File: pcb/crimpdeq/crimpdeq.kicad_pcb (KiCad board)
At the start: 2 copper layers, 23 x 63.8 mm, 49 parts, among them J2 USB4105-GF-A, Q1 SS8550, Q2 DMG3415U, SW1 SW_Push, SW2 SW_Push, U1 ESP32-C3-MINI-1, U2 MCP73831T-2ACI/OT, U3 HX711, U4 Rust_Board, U6 SY8088

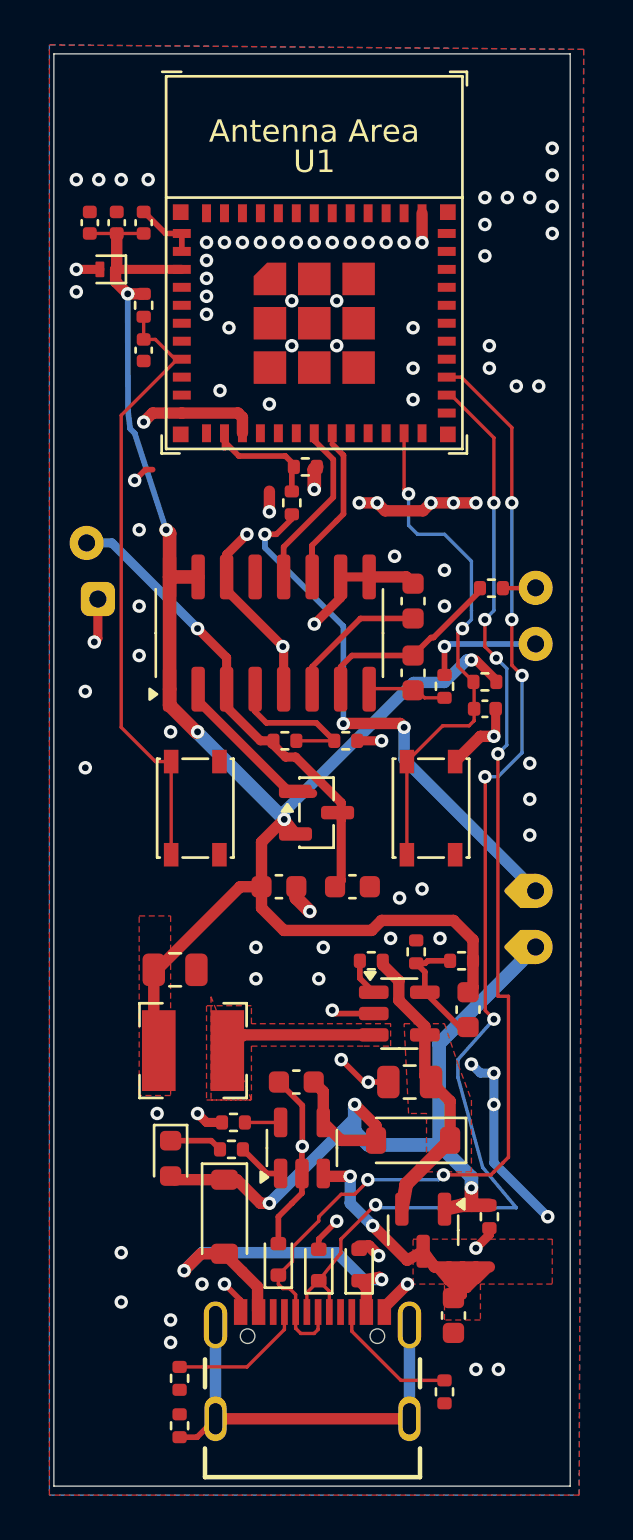
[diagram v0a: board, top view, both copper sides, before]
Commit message: feat: Add rbg led and route it
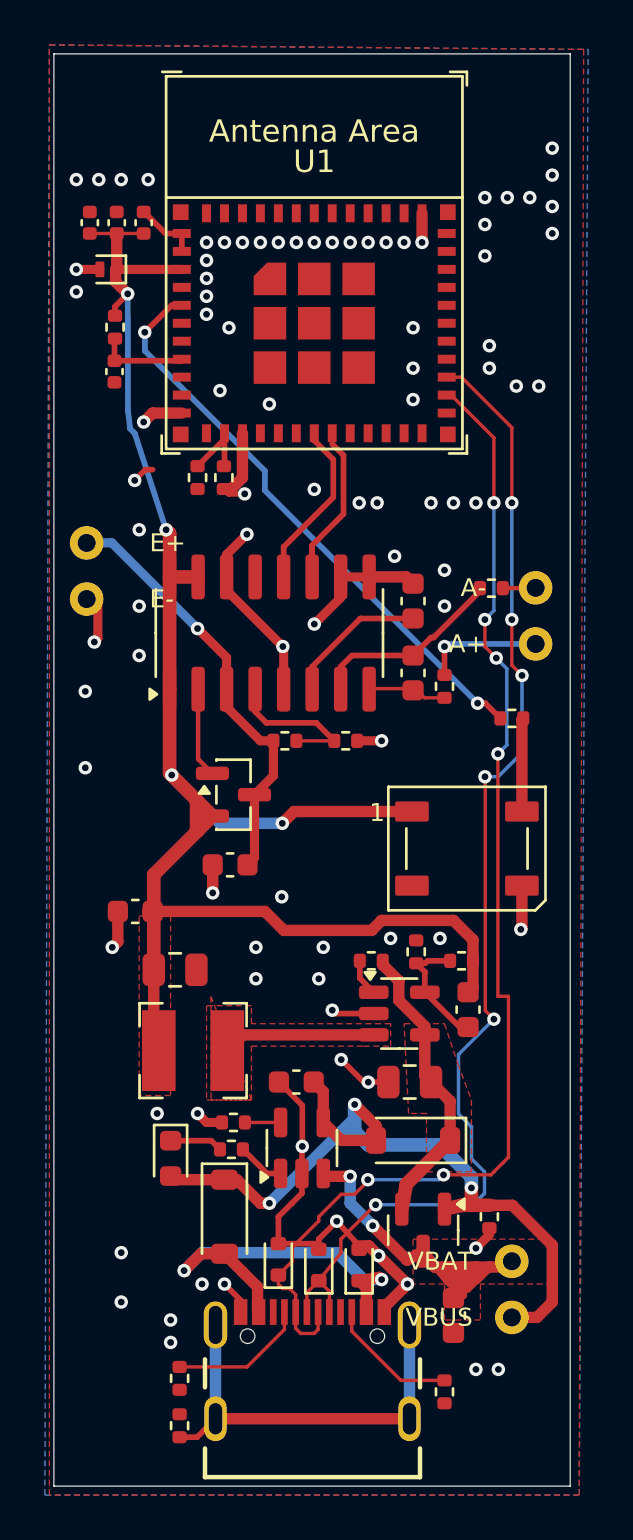
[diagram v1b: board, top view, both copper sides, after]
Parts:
- removed C14: 1nF 10V, Capacitor_SMD:C_0402_1005Metric
- removed R10: 10kR 1%, Resistor_SMD:R_0402_1005Metric
- removed SW1, SW2: SW_Push, Button_Switch_SMD:SW_SPST_PTS810
- removed U4: Rust_Board, Rust_Board:Rust_Board
- added D4: WS2812B, LED_SMD:LED_WS2812B_PLCC4_5.0x5.0mm_P3.2mm, F.Cu at (147.6, 81.8)
- added J3: Loadcell_Pads, External_Cable_Pads_Left, F.Cu at (130.7, 69.4)
- added J4: Power_Sense_Pads, External_Cable_Pads_Right, F.Cu at (150.7, 78.2)
- added R13: 0R 1%, Resistor_SMD:R_0402_1005Metric, F.Cu at (149.6, 76.0)
- moved C9 6.49 mm to (132.8, 84.6), turned to 180 degrees
- moved C10 5.54 mm to (137.1, 82.5), turned to 180 degrees
- moved R12 4.35 mm to (135.6, 65.3)
- moved Q1 3.79 mm to (137.2, 79.4)
- moved R11 3.66 mm to (136.8, 65.3), turned to -90 degrees
- moved C3 1.61 mm to (131.9, 60.5)
- moved R1 1.61 mm to (131.9, 58.6)
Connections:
- U1 pad 49: GND -> (no net)
- U1 pad 5: unconnected-(U1-GPIO2/ADC1_CH2-Pad5) -> IO2_LED
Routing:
- net IO2_LED: track 0.00 -> 26.1 mm, vias 0 -> 2
- net 59: track 24.1 -> 0.00 mm, vias 3 -> 0
- net CHIP_PU: track 27.7 -> 4.02 mm
- net IO9_BOOT: track 23.2 -> 0.00 mm, vias 2 -> 0
- net VSYS: track 0.00 -> 13.1 mm
- net +5V: track 12.0 -> 0.00 mm
- net GND: track 71.3 -> 61.0 mm, vias 104 -> 92
- net +BATT: track 15.4 -> 21.9 mm
- net 18: track 4.78 -> 0.00 mm
- net 5: track 4.40 -> 0.00 mm
- net Net-(D4-DIN): track 0.00 -> 4.17 mm
- net Net-(Q1-B): track 7.56 -> 4.53 mm
- net USB_D+: track 50.4 -> 53.3 mm
- net 17: track 2.44 -> 0.00 mm
- net Net-(D8-A): track 15.2 -> 17.6 mm
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
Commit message: fix: resolve schematic and layout rule violations
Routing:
- net GND: track 61.0 -> 55.9 mm
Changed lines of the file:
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@@
 			)
 		)
-		(attr through_hole)
+		(attr through_hole board_only)
 		(duplicate_pad_numbers_are_jumpers no)
-		(fp_text user "VBAT"
-			(at -2.8 22 0)
+		(fp_text user "A-"
+			(at -0.4 -9.4 0)
 			(layer "F.SilkS")
 			(effects
@@
 					(thickness 0.12)
 				)
-				(justify right)
 			)
 		)
-		(fp_text user "VBUS"
-			(at -2.8 24.5 0)
+		(fp_text user "A+"
+			(at -0.4 -4.1 0)
 			(layer "F.SilkS")
 			(effects
@@
 					(thickness 0.12)
 				)
-				(justify right)
 			)
 		)
-		(fp_text user "A-"
-			(at -2.2 -8 0)
+		(fp_text user "VBUS"
+			(at -0.4 25.9 0)
 			(layer "F.SilkS")
 			(effects
@@
 					(thickness 0.12)
 				)
-				(justify right)
 			)
 		)
-		(fp_text user "A+"
-			(at -2.2 -5.5 0)
+		(fp_text user "VBAT"
+			(at 0 18.6 0)
 			(layer "F.SilkS")
 			(effects
@@
 					(thickness 0.12)
 				)
-				(justify right)
 			)
 		)
@@
 			)
 		)
-		(attr through_hole)
+		(attr through_hole board_only)
 		(duplicate_pad_numbers_are_jumpers no)
 		(fp_text user "E+"
-			(at 2.8 -1.25 0)
+			(at 0 -3 0)
 			(layer "F.SilkS")
 			(effects
@@
 					(thickness 0.12)
 				)
-				(justify left)
 			)
 		)
 		(fp_text user "E-"
-			(at 2.8 1.25 0)
+			(at 0 3 0)
 			(layer "F.SilkS")
 			(effects
@@
 					(thickness 0.12)
 				)
-				(justify left)
 			)
 		)
@@
 	)
 	(segment
-		(start 147.8025 94.1975)
-		(end 147.805 94.2)
-		(width 0.1524)
-		(layer "B.Cu")
-		(net "USB_D+")
-	)
-	(segment
 		(start 148.8 89.4)
 		(end 147.2238 90.9762)
@@
 	)
 	(segment
-		(start 141.8 98.4)
-		(end 142.8 99.5)
-		(width 0.254)
-		(layer "F.Cu")
-		(net "GND")
-	)
-	(segment
 		(start 137.6 63.3)
 		(end 137.6 65.279999)
@@
 	)
 	(segment
-		(start 143.666841 99.933159)
-		(end 144.950485 101.2)
-		(width 0.508)
-		(layer "F.Cu")
-		(net "GND")
-	)
-	(segment
 		(start 143.92 102.445)
 		(end 143.92 102.230485)
@@
 	)
 	(segment
-		(start 139.2 99.4)
-		(end 141 99.4)
-		(width 0.254)
-		(layer "F.Cu")
-		(net "GND")
-	)
-	(segment
 		(start 139.435 72.835)
 		(end 139.4 72.8)
@@
 		(hatch edge 0.5)
 		(priority 5)
-		(connect_pads
+		(connect_pads yes
 			(clearance 0.5)
 		)
@@
 		(hatch edge 0.5)
 		(priority 2)
-		(connect_pads
+		(connect_pads yes
 			(clearance 0.5)
 		)

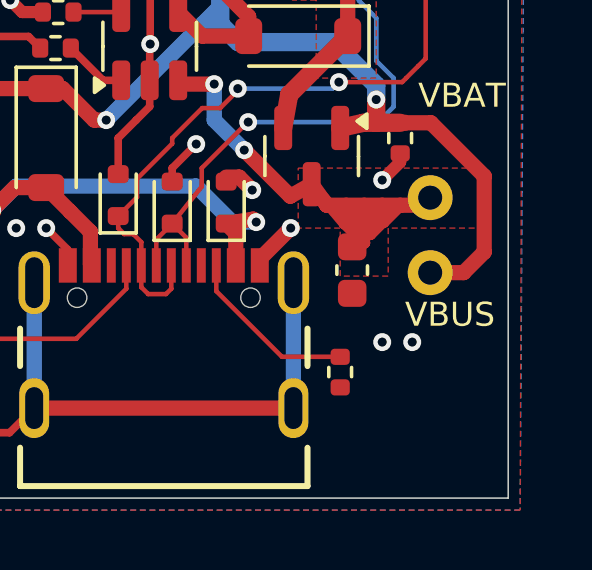
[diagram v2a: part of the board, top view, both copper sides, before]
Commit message: fix: allow charging while switched off
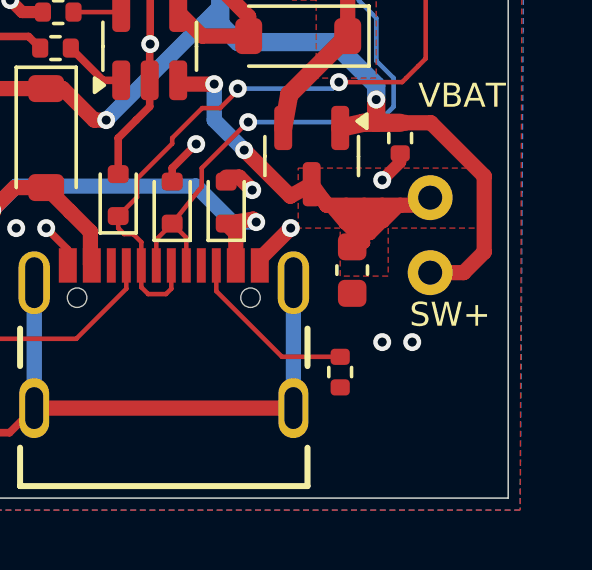
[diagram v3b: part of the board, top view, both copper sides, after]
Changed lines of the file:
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@@
 			)
 		)
-		(fp_text user "VBUS"
+		(fp_text user "SW+"
 			(at -0.4 25.9 0)
 			(layer "F.SilkS")
@@
 			(remove_unused_layers no)
 			(net "VBUS")
-			(pinfunction "VBUS")
+			(pinfunction "SW+/VBUS")
 			(pintype "passive")
 		)
@@
 			)
 		)
-		(property "Description" ""
+		(property "Description" "DNP for charge-while-off wiring; switch output feeds SW+/VBUS pad instead."
 			(at 0 0 90)
 			(layer "F.Fab")
@@
 			)
 		)
-		(attr smd)
+		(attr smd dnp)
 		(duplicate_pad_numbers_are_jumpers no)
 		(fp_line

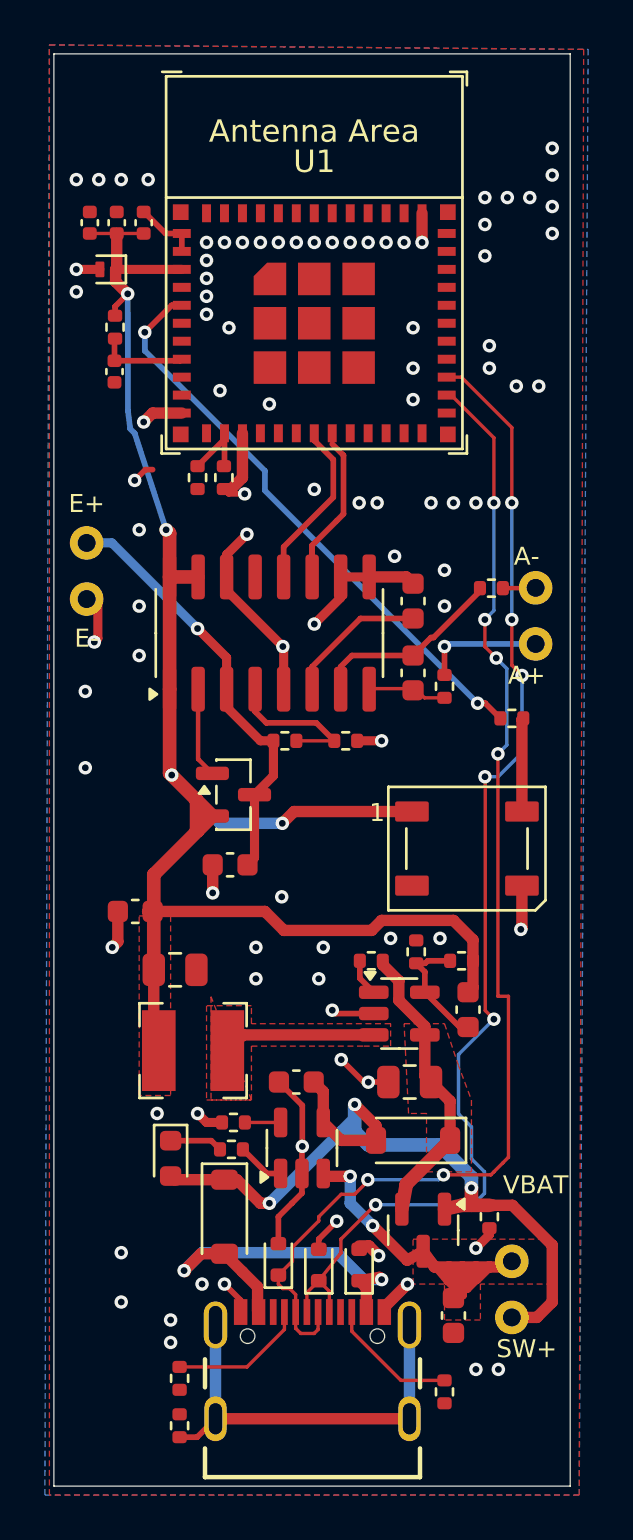
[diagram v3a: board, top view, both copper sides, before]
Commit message: feat: Add battery gauge, review schematic/pcb
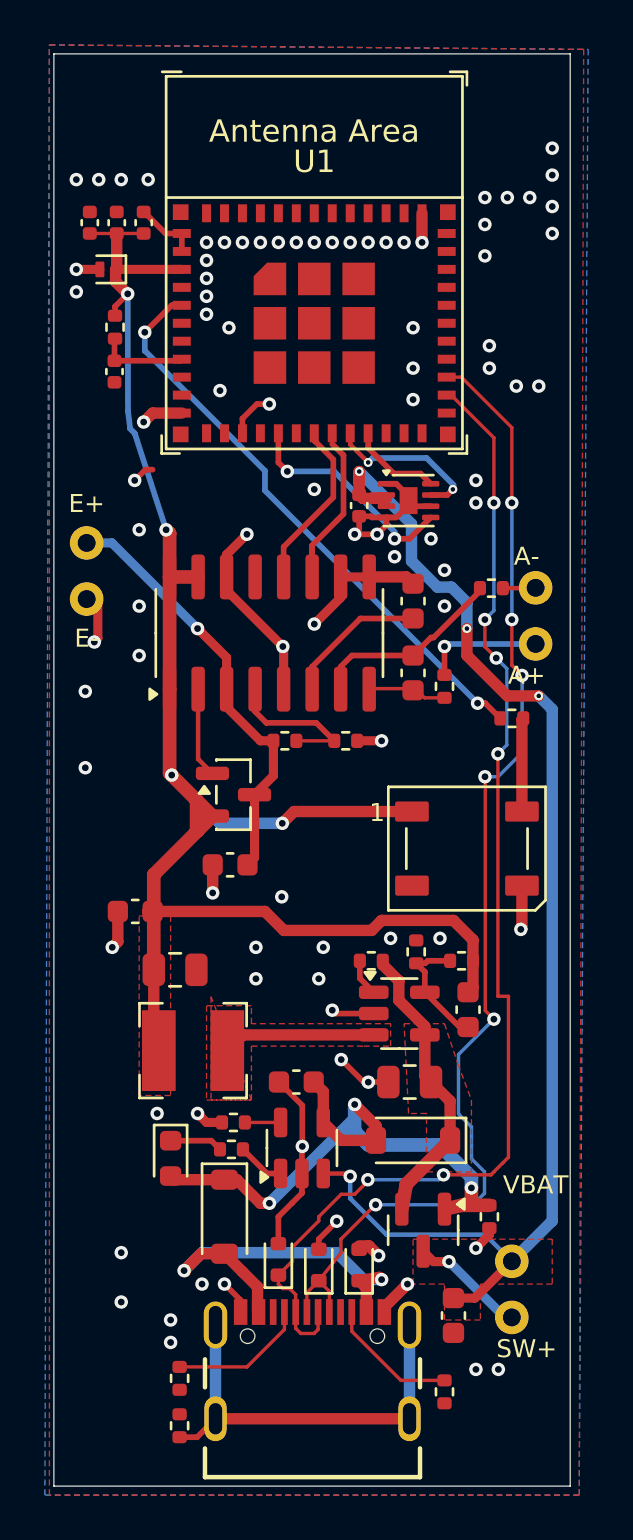
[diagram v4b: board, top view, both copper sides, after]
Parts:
- removed R11: 10kR 1%, Resistor_SMD:R_0402_1005Metric
- removed R12: 33kR 1%, Resistor_SMD:R_0402_1005Metric
- added C18: 100nF 10V, Capacitor_SMD:C_0402_1005Metric, F.Cu at (142.8, 66.5)
- added U5: MAX17048G+T10, Package_DFN_QFN:TDFN-8-1EP_2x2mm_P0.5mm_EP0.8x1.2mm, F.Cu at (145.0, 66.3)
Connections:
- J4 pad 4: VBUS -> SW_BATT
- Q2 pad 3: +BATT -> SW_BATT
- U1 pad 13: IO1_ADC -> unconnected-(U1-GPIO1/ADC1_CH1/XTAL_32K_N-Pad13)
- U1 pad 16: unconnected-(U1-GPIO10-Pad16) -> IO10_ALRT
- U1 pad 20: unconnected-(U1-GPIO6-Pad20) -> IO6_SDA
- U1 pad 21: unconnected-(U1-GPIO7-Pad21) -> IO7_SCL
- U1 pad 23: IO9_BOOT -> unconnected-(U1-GPIO9-Pad23)
- U1 pad 30: IO20_RX -> unconnected-(U1-GPIO20/U0RXD-Pad30)
- U1 pad 31: IO21_TX -> unconnected-(U1-GPIO21/U0TXD-Pad31)
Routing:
- net +BATT: track 21.9 -> 59.2 mm, vias 2 -> 4
- net IO10_ALRT: track 0.00 -> 10.1 mm, vias 0 -> 2
- net VBUS: track 36.4 -> 28.3 mm
- net IO6_SDA: track 0.00 -> 7.31 mm, vias 0 -> 2
- net GND: track 55.9 -> 62.0 mm, vias 92 -> 91
- net SW_BATT: track 0.00 -> 5.17 mm, vias 0 -> 1
- net IO7_SCL: track 0.00 -> 4.10 mm
- net IO1_ADC: track 3.44 -> 0.00 mm

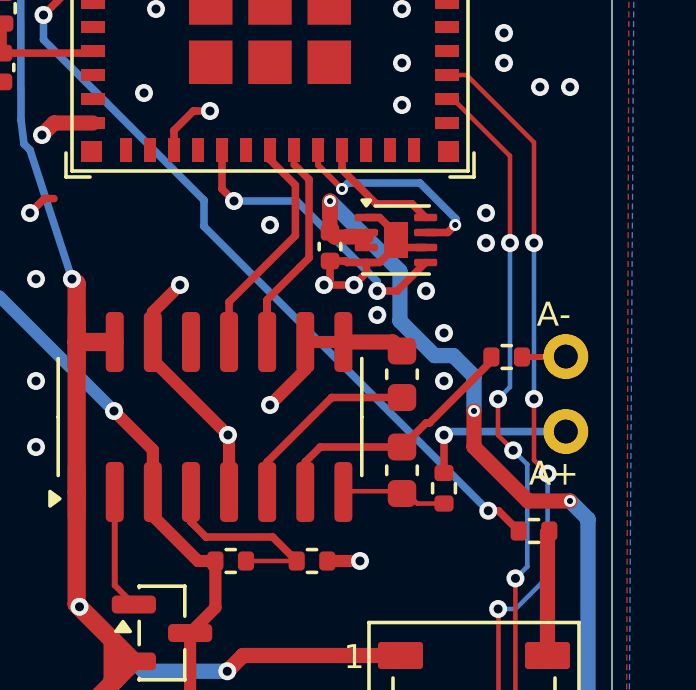
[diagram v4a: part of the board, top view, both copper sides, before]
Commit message: fix: Via diameters
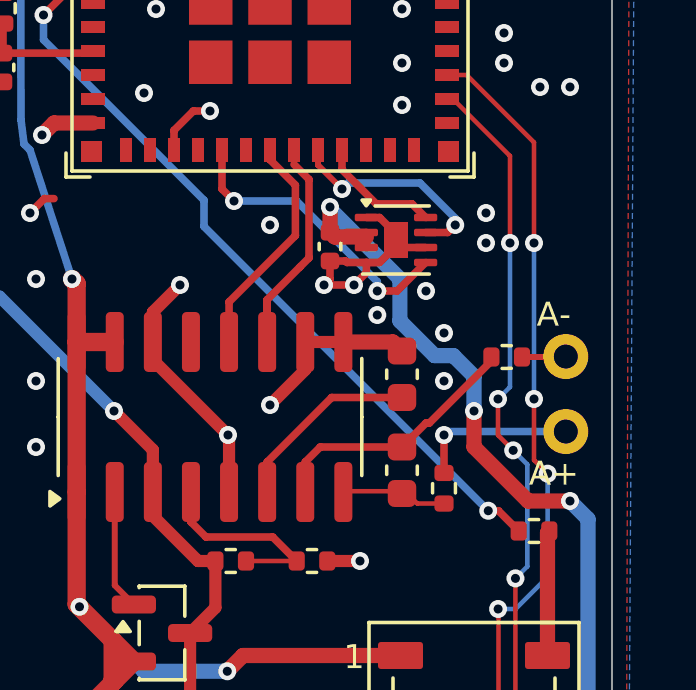
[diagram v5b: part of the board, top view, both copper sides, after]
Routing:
- net +BATT: track 59.2 -> 58.3 mm
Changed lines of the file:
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@@
+	)
+	(segment
+		(start 142.8 66.04)
+		(end 142.8 65.266318)
+		(width 0.508)
+		(layer "F.Cu")
+		(net "+BATT")
 	)
 	(segment
@@
 	)
 	(segment
-		(start 142.8 65.004)
-		(end 142.8 65.52)
-		(width 0.508)
-		(layer "F.Cu")
-		(net "+BATT")
-	)
-	(segment
 		(start 144.0125 66.2)
 		(end 144.0125 66.05)
 		(width 0.254)
-		(layer "F.Cu")
-		(net "+BATT")
-	)
-	(segment
-		(start 142.8 65.004)
-		(end 142.8 66.04)
-		(width 0.508)
 		(layer "F.Cu")
 		(net "+BATT")
@@
 	)
 	(segment
-		(start 142.814318 65.52)
-		(end 142.8 65.52)
-		(width 0.254)
+		(start 142.8 65.266318)
+		(end 142.766841 65.233159)
+		(width 0.508)
 		(layer "F.Cu")
 		(net "+BATT")
@@
 	)
 	(via
-		(at 142.8 65.004)
-		(size 0.4)
-		(drill 0.2)
+		(at 142.8 65.2)
+		(size 0.6)
+		(drill 0.3)
 		(layers "F.Cu" "B.Cu")
 		(net "+BATT")
@@
 	(via
 		(at 147.6 72)
-		(size 0.4)
-		(drill 0.2)
+		(size 0.6)
+		(drill 0.3)
 		(layers "F.Cu" "B.Cu")
 		(net "+BATT")
@@
 	(via
 		(at 150.8 75)
-		(size 0.4)
-		(drill 0.2)
+		(size 0.6)
+		(drill 0.3)
 		(layers "F.Cu" "B.Cu")
 		(net "+BATT")
@@
 	)
 	(segment
-		(start 145.130651 67.334651)
-		(end 142.8 65.004)
-		(width 0.508)
-		(layer "B.Cu")
-		(net "+BATT")
-	)
-	(segment
 		(start 146.287682 70.154)
 		(end 145.130651 68.996969)
@@
 		(start 149.6 100.185)
 		(end 151.4 98.385)
+		(width 0.508)
+		(layer "B.Cu")
+		(net "+BATT")
+	)
+	(segment
+		(start 145.130651 67.596969)
+		(end 142.766841 65.233159)
 		(width 0.508)
 		(layer "B.Cu")
@@
 	)
 	(segment
-		(start 145.130651 68.996969)
-		(end 145.130651 67.334651)
-		(width 0.508)
-		(layer "B.Cu")
-		(net "+BATT")
-	)
-	(segment
 		(start 151.4 98.385)
 		(end 151.4 75.6)
@@
 	)
 	(segment
+		(start 145.130651 68.996969)
+		(end 145.130651 67.596969)
+		(width 0.508)
+		(layer "B.Cu")
+		(net "+BATT")
+	)
+	(segment
 		(start 144.017789 99)
 		(end 148.415 99)
@@
 	(via
 		(at 146.9738 65.8)
-		(size 0.4)
-		(drill 0.2)
+		(size 0.6)
+		(drill 0.3)
 		(layers "F.Cu" "B.Cu")
 		(net "IO6_SDA")
@@
 	(via
 		(at 143.2 64.6)
-		(size 0.4)
-		(drill 0.2)
+		(size 0.6)
+		(drill 0.3)
 		(layers "F.Cu" "B.Cu")
 		(net "IO6_SDA")
